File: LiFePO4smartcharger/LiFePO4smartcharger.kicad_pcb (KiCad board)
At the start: 2 copper layers, 99.3 x 98.6 mm, 100 parts, among them J1 Conn_01x02, J10 Conn_01x01, J11 Conn_01x01, J12 Conn_01x04, J13 Conn_01x01, J2 Conn_02x03_Odd_Even, J3 Conn_01x02, J4 Conn_01x02, J5 Barrel_Jack, J6 Conn_01x01, J7 Conn_01x01, J8 Conn_01x02, J9 Conn_01x02, Q1 TIP42, Q2 TIP41, Q3 2N3906, Q4 TIP41C, T1 Transformer_1P1Sdotted, U1 ATMEGA328P-PU, U2 LM358, U3 LCD-016N002L, U4 TL494, U9 LM7805_TO220, X3 16MHz

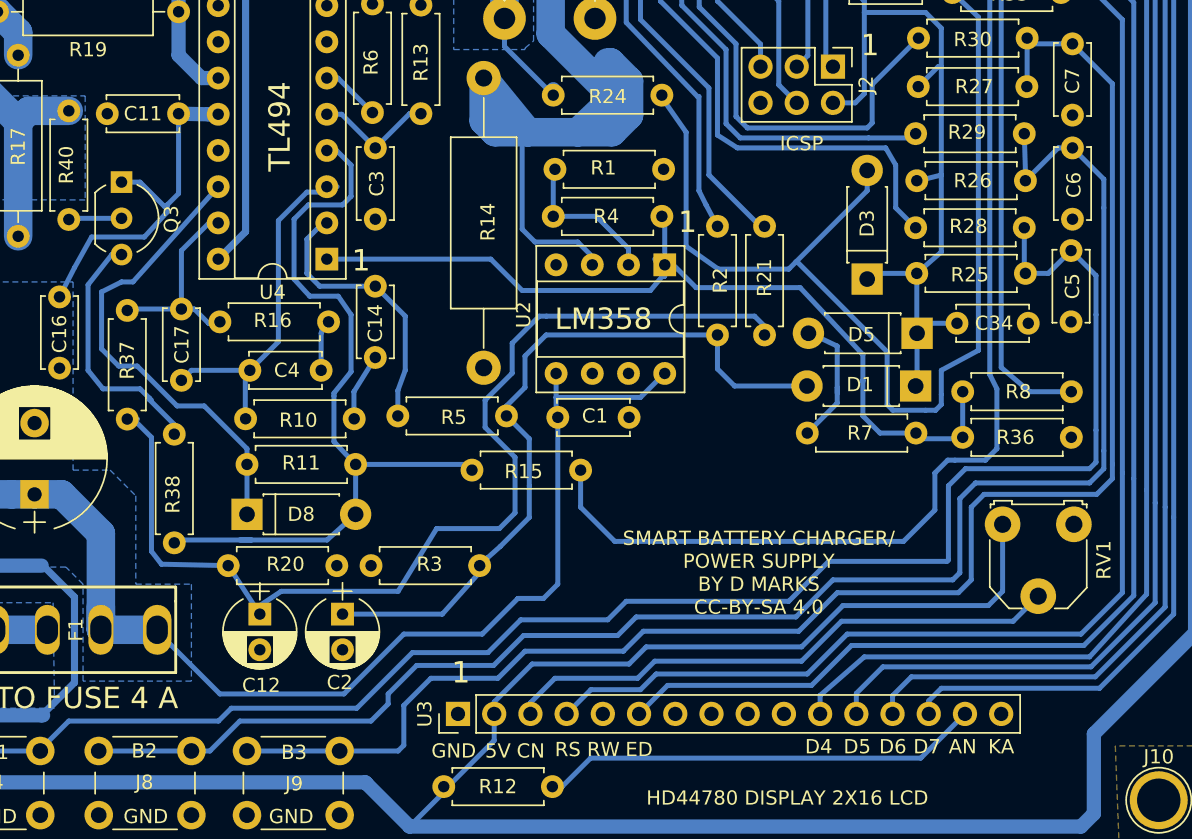
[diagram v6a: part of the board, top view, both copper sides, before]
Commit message: Added compensation for shunt resistor voltage drop
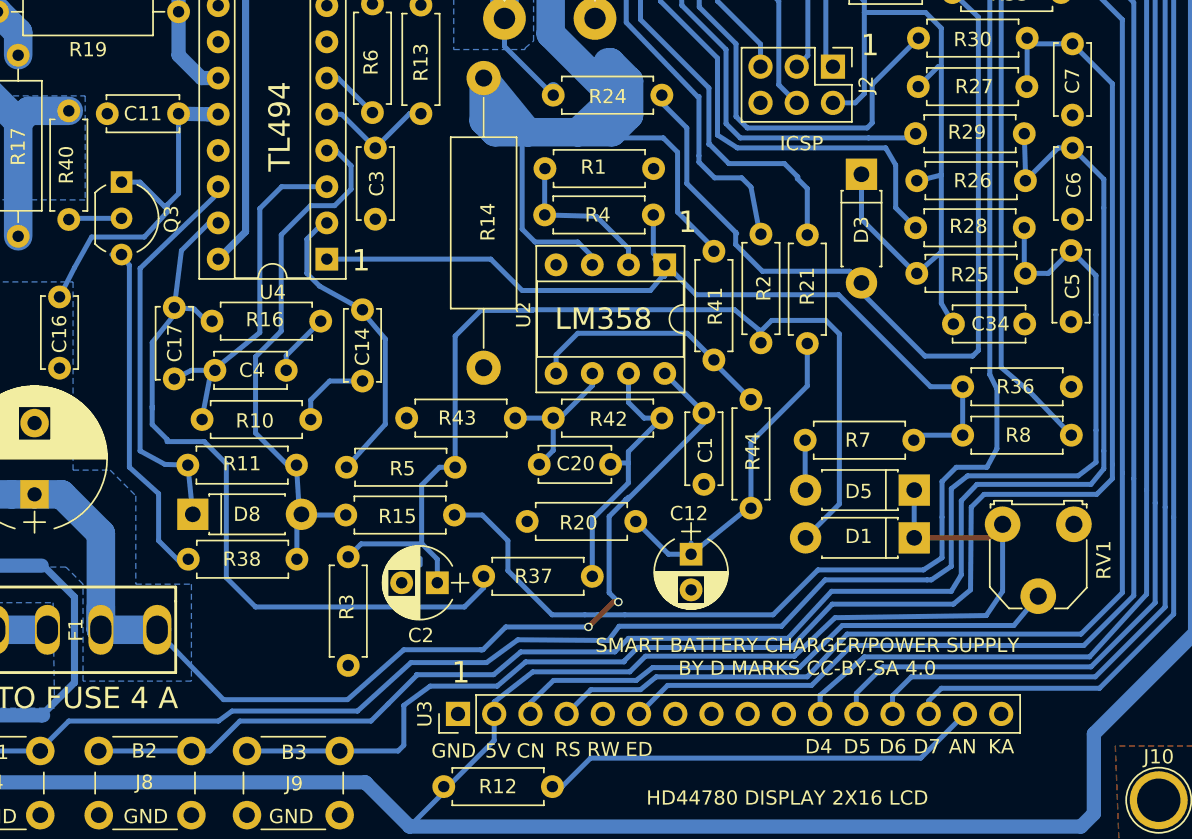
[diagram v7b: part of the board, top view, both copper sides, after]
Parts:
- added C20: 22 pF, Capacitors_THT:C_Disc_D5.0mm_W2.5mm_P5.00mm, F.Cu at (94.3, 101.9)
- added R41: 450k, Resistors_THT:R_Axial_DIN0207_L6.3mm_D2.5mm_P7.62mm_Horizontal, F.Cu at (106.5, 87.0)
- added R42: 2k2, Resistors_THT:R_Axial_DIN0207_L6.3mm_D2.5mm_P7.62mm_Horizontal, F.Cu at (102.9, 98.7)
- added R43: 10k, Resistors_THT:R_Axial_DIN0207_L6.3mm_D2.5mm_P7.62mm_Horizontal, F.Cu at (85.0, 98.7)
- added R44: 100k, Resistors_THT:R_Axial_DIN0207_L6.3mm_D2.5mm_P7.62mm_Horizontal, F.Cu at (109.2, 97.3)
- R23, R33: value 3k3 -> 2k7
- moved R37 31.2 mm to (90.4, 109.8), turned to 0 degrees
- moved C12 30.5 mm to (105.0, 108.2)
- moved R20 13.7 mm to (93.5, 105.9), turned to 0 degrees
- moved D5 11.0 mm to (120.6, 103.7)
- moved D1 10.7 mm to (120.6, 107.0)
- moved C1 10.3 mm to (105.8, 98.3), turned to 270 degrees
- moved R15 9.39 mm to (88.3, 105.5)
- moved R38 8.68 mm to (77.3, 108.5), turned to 180 degrees
- moved D3 7.36 mm to (116.9, 81.5), turned to 270 degrees
- moved R3 7.18 mm to (80.9, 116.0), turned to 90 degrees
- moved C2 7.00 mm to (87.2, 110.2), turned to 180 degrees
- moved R5 5.09 mm to (88.4, 102.1)
- moved R11 4.15 mm to (69.7, 102.0)
- moved D8 3.80 mm to (70.0, 105.4)
- moved R36 3.55 mm to (124.0, 96.5)
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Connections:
- R37 pad 2: Net-(C12-Pad1) -> Net-(C20-Pad2)
- U2 pad 5: +24V -> Net-(R41-Pad2)
- U2 pad 6: GND -> Net-(C20-Pad1)
- U2 pad 7: (no net) -> Net-(C20-Pad2)
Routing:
- net Net-(C12-Pad1): track 77.3 -> 24.5 mm
- net Net-(C17-Pad1): track 15.1 -> 54.5 mm
- net Net-(C20-Pad2): track 0.00 -> 20.6 mm
- net Net-(R41-Pad2): track 0.00 -> 19.0 mm
- net Net-(C2-Pad1): track 53.0 -> 70.8 mm
- net A0: track 80.5 -> 63.6 mm
- net Net-(D8-Pad2): track 57.3 -> 40.5 mm
- net SHUTDOWN: track 81.7 -> 95.0 mm
- net CURRENTSHUNT: track 181.2 -> 194.4 mm
- net Net-(C20-Pad1): track 0.00 -> 10.9 mm
- net +5V: track 412.1 -> 419.5 mm
- net Net-(Q3-Pad3): track 18.0 -> 24.6 mm
- net Net-(D5-Pad2): track 9.59 -> 3.51 mm
- net Net-(D8-Pad1): track 33.0 -> 27.9 mm
- net VOLTAGESET: track 37.4 -> 41.7 mm
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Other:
- board text added: "SMART BATTERY CHARGER/POWER SUPPLY BY D MARKS CC-BY-SA 4.0"
- board text removed: "SMART BATTERY CHARGER/ POWER SUPPLY BY D MARKS CC-BY-SA 4.0"

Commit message: JLCPCB 2021-03-26
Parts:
- added J14: Conn_01x02, Connectors_Terminal_Blocks:TerminalBlock_bornier-2_P5.08mm, F.Cu at (102.8, 50.5)
- J5: value Barrel_Jack -> Conn_01x02; footprint Connectors:BARREL_JACK -> Connectors_Terminal_Blocks:TerminalBlock_bornier-2_P5.08mm
- R41: value 450k -> 470k
- moved J5 3.72 mm to (47.7, 112.7), turned to 270 degrees
- moved Q1 3.15 mm to (52.1, 68.0)
- moved D2 2.24 mm to (61.5, 47.0)
- moved X3 2.15 mm to (119.5, 51.7)
- moved R34 2.05 mm to (53.0, 96.3)
- moved D11 1.53 mm to (51.5, 106.8)
- moved C30 0.96 mm to (118.2, 47.2)
- moved C19 0.85 mm to (125.3, 47.2)
- moved U9 0.80 mm to (46.9, 101.5)
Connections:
- Q4 pad 2: Net-(Q4-Pad2) -> Net-(J14-Pad2)
- R31 pad 2: Net-(Q4-Pad2) -> Net-(J14-Pad1)
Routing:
- net Net-(Q4-Pad2): track 19.0 -> 0.00 mm
- net Net-(J14-Pad2): track 0.00 -> 18.5 mm
- net Net-(J14-Pad1): track 0.00 -> 7.75 mm
- net DRAINBASE: track 34.5 -> 30.5 mm
- net Net-(Q1-Pad2): track 20.3 -> 24.0 mm
- net CURRENTSHUNT: track 194.4 -> 191.0 mm
- net +24V: track 114.6 -> 117.4 mm
- net Net-(F1-Pad2): track 9.66 -> 12.5 mm
- net Net-(Q1-Pad1): track 10.6 -> 8.67 mm
- net +5V: track 419.5 -> 421.4 mm
- net Net-(C30-Pad2): track 10.6 -> 12.4 mm
- net CURRENTSET: track 37.5 -> 38.4 mm
- net Net-(Q4-Pad3): track 5.25 -> 4.43 mm
- net VOLTAGESET: track 41.7 -> 42.2 mm
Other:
- board text added: "18-26V INPUT"
- board text added: "PWR GND"
- board text removed: "18-26V PIN +"
